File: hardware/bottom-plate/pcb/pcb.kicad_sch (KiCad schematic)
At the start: 83 parts, among them SW1 MT-0-102-A101-M200-RS+PJ, SW2 TS4535TP 250GF 009, SW3 TS4535TP 250GF 009

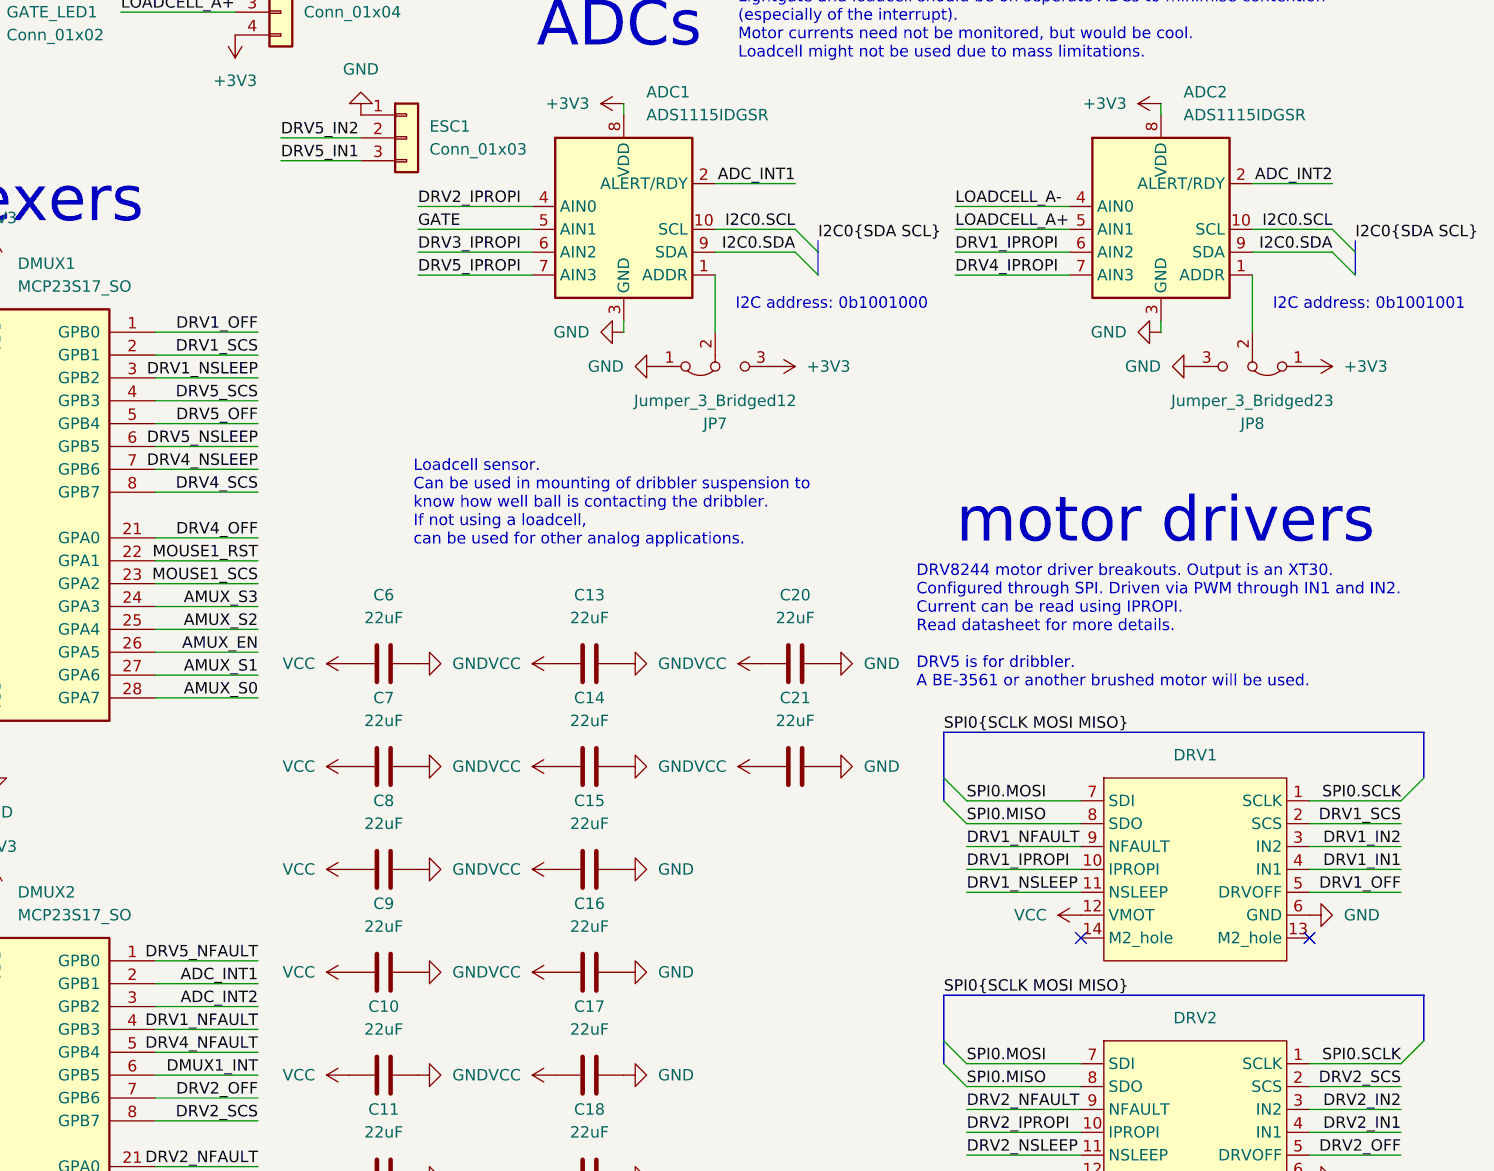
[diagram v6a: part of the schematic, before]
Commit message: fixed up cmake v2, added bottom pcb pinmaps, fixed bottom pcb pin naming in schematic
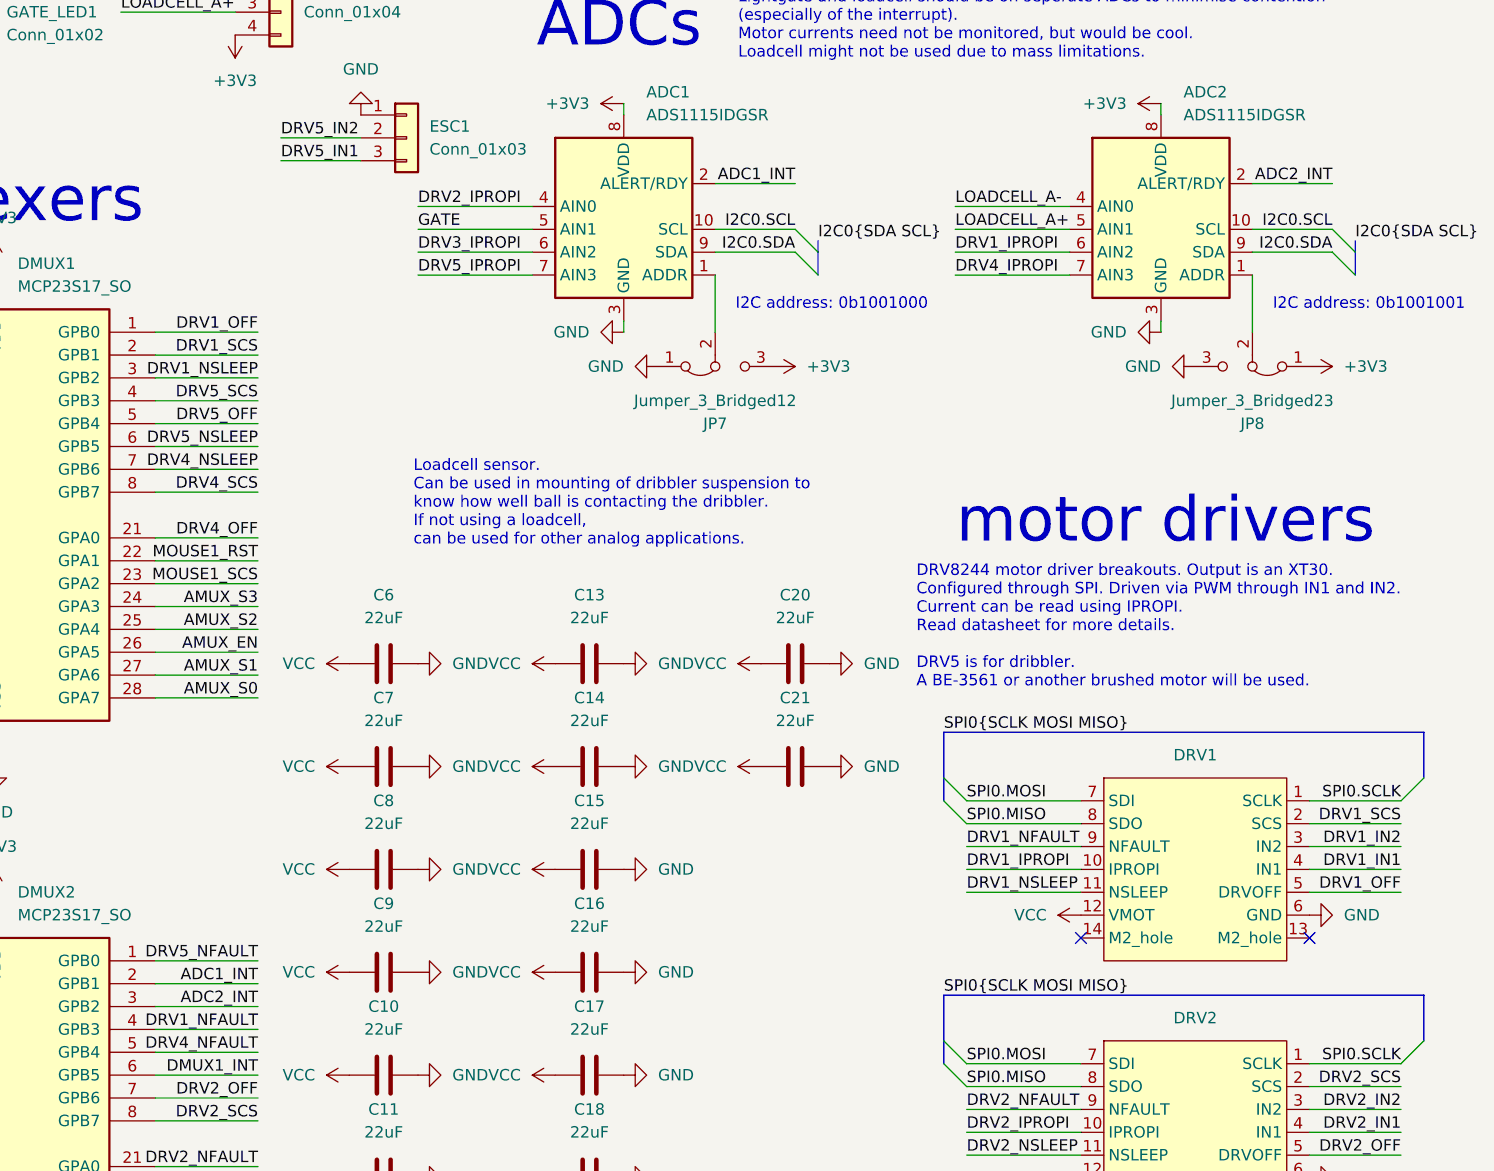
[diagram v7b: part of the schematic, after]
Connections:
- net ADC_INT1 renamed ADC1_INT
- net ADC_INT2 renamed ADC2_INT
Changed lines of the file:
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@@
 		)
 	)
-	(label "ADC_INT2"
+	(label "ADC2_INT"
 		(at 184.15 135.89 180)
 		(effects
@@
 		)
 	)
-	(label "ADC_INT2"
+	(label "ADC2_INT"
 		(at 303.53 44.45 180)
 		(effects
@@
 		)
 	)
-	(label "ADC_INT1"
+	(label "ADC1_INT"
 		(at 184.15 133.35 180)
 		(effects
@@
 		)
 	)
-	(label "ADC_INT1"
+	(label "ADC1_INT"
 		(at 243.84 44.45 180)
 		(effects

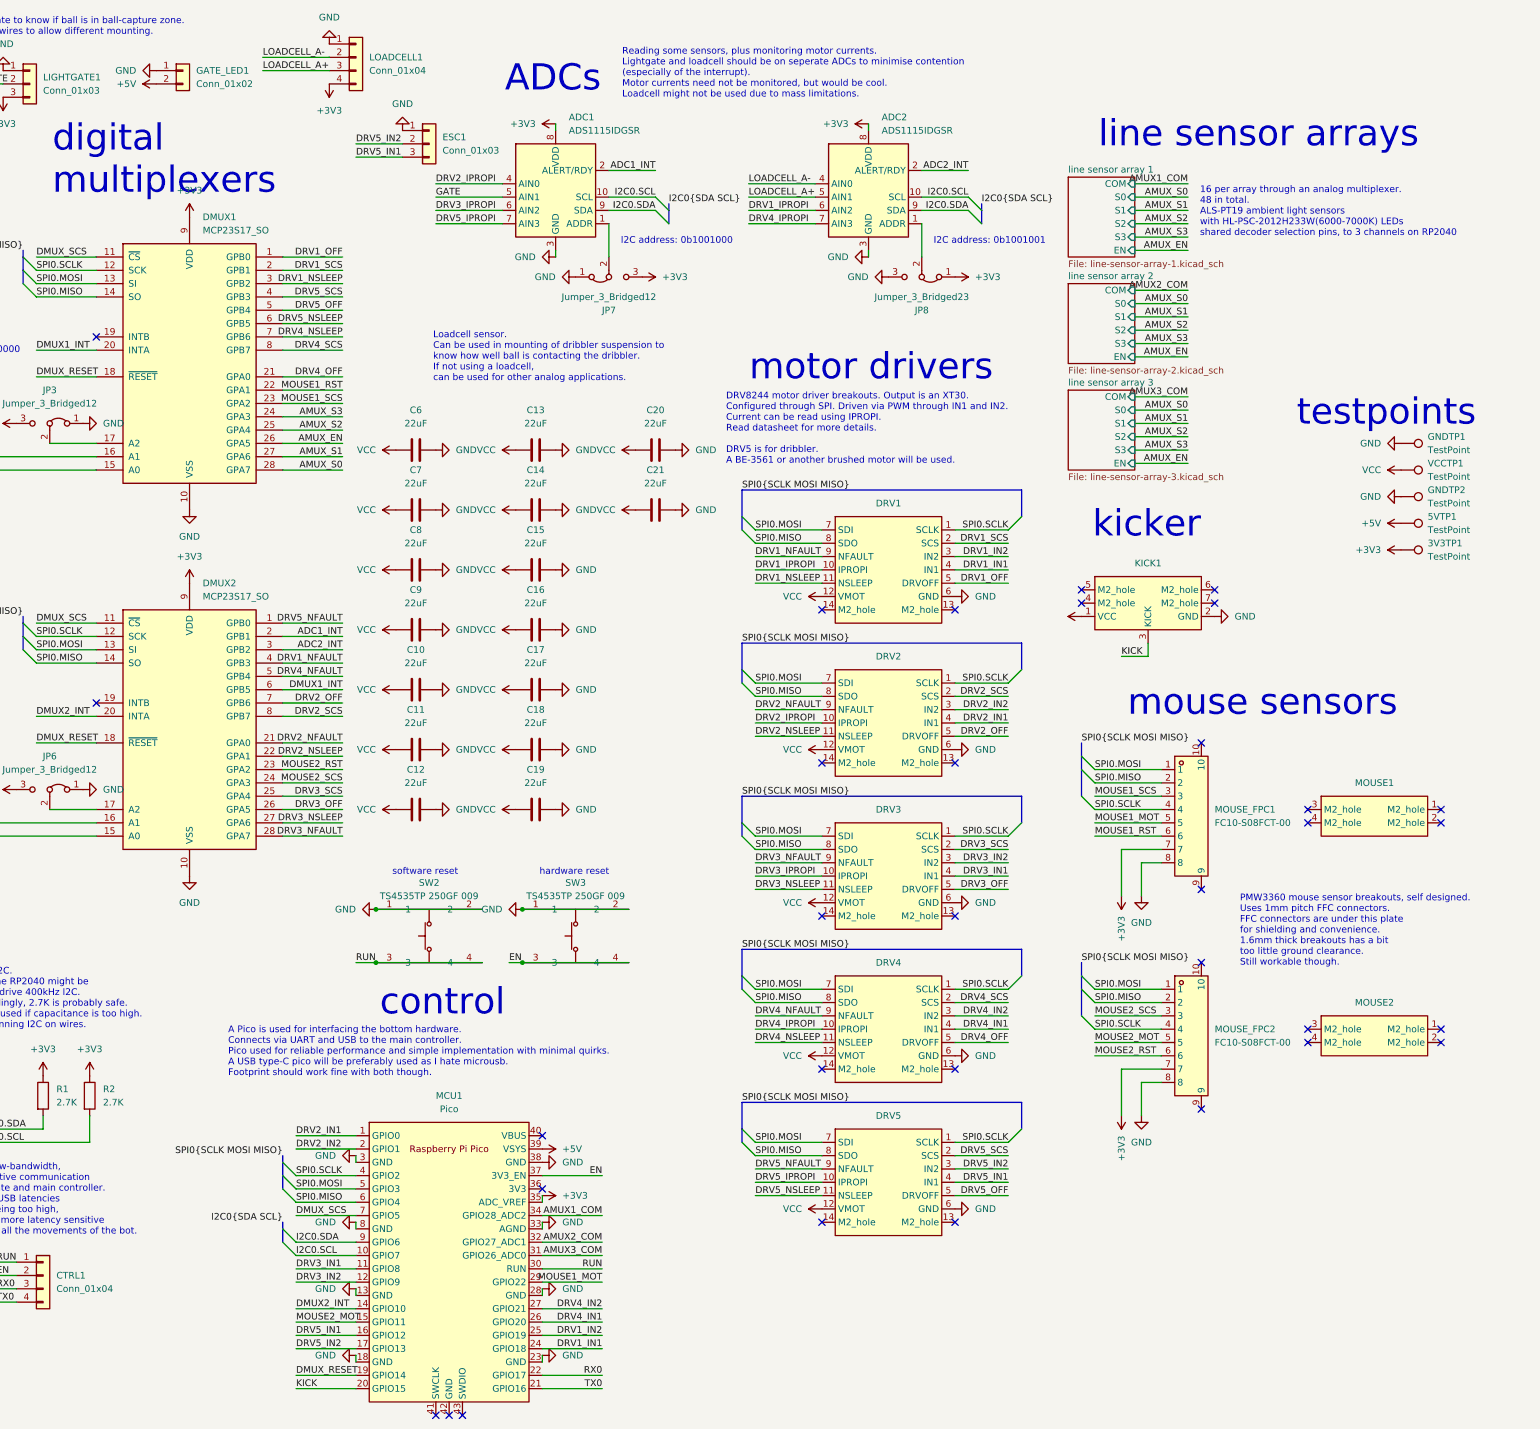
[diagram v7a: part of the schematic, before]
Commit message: bottom pcb fixed, im stupid
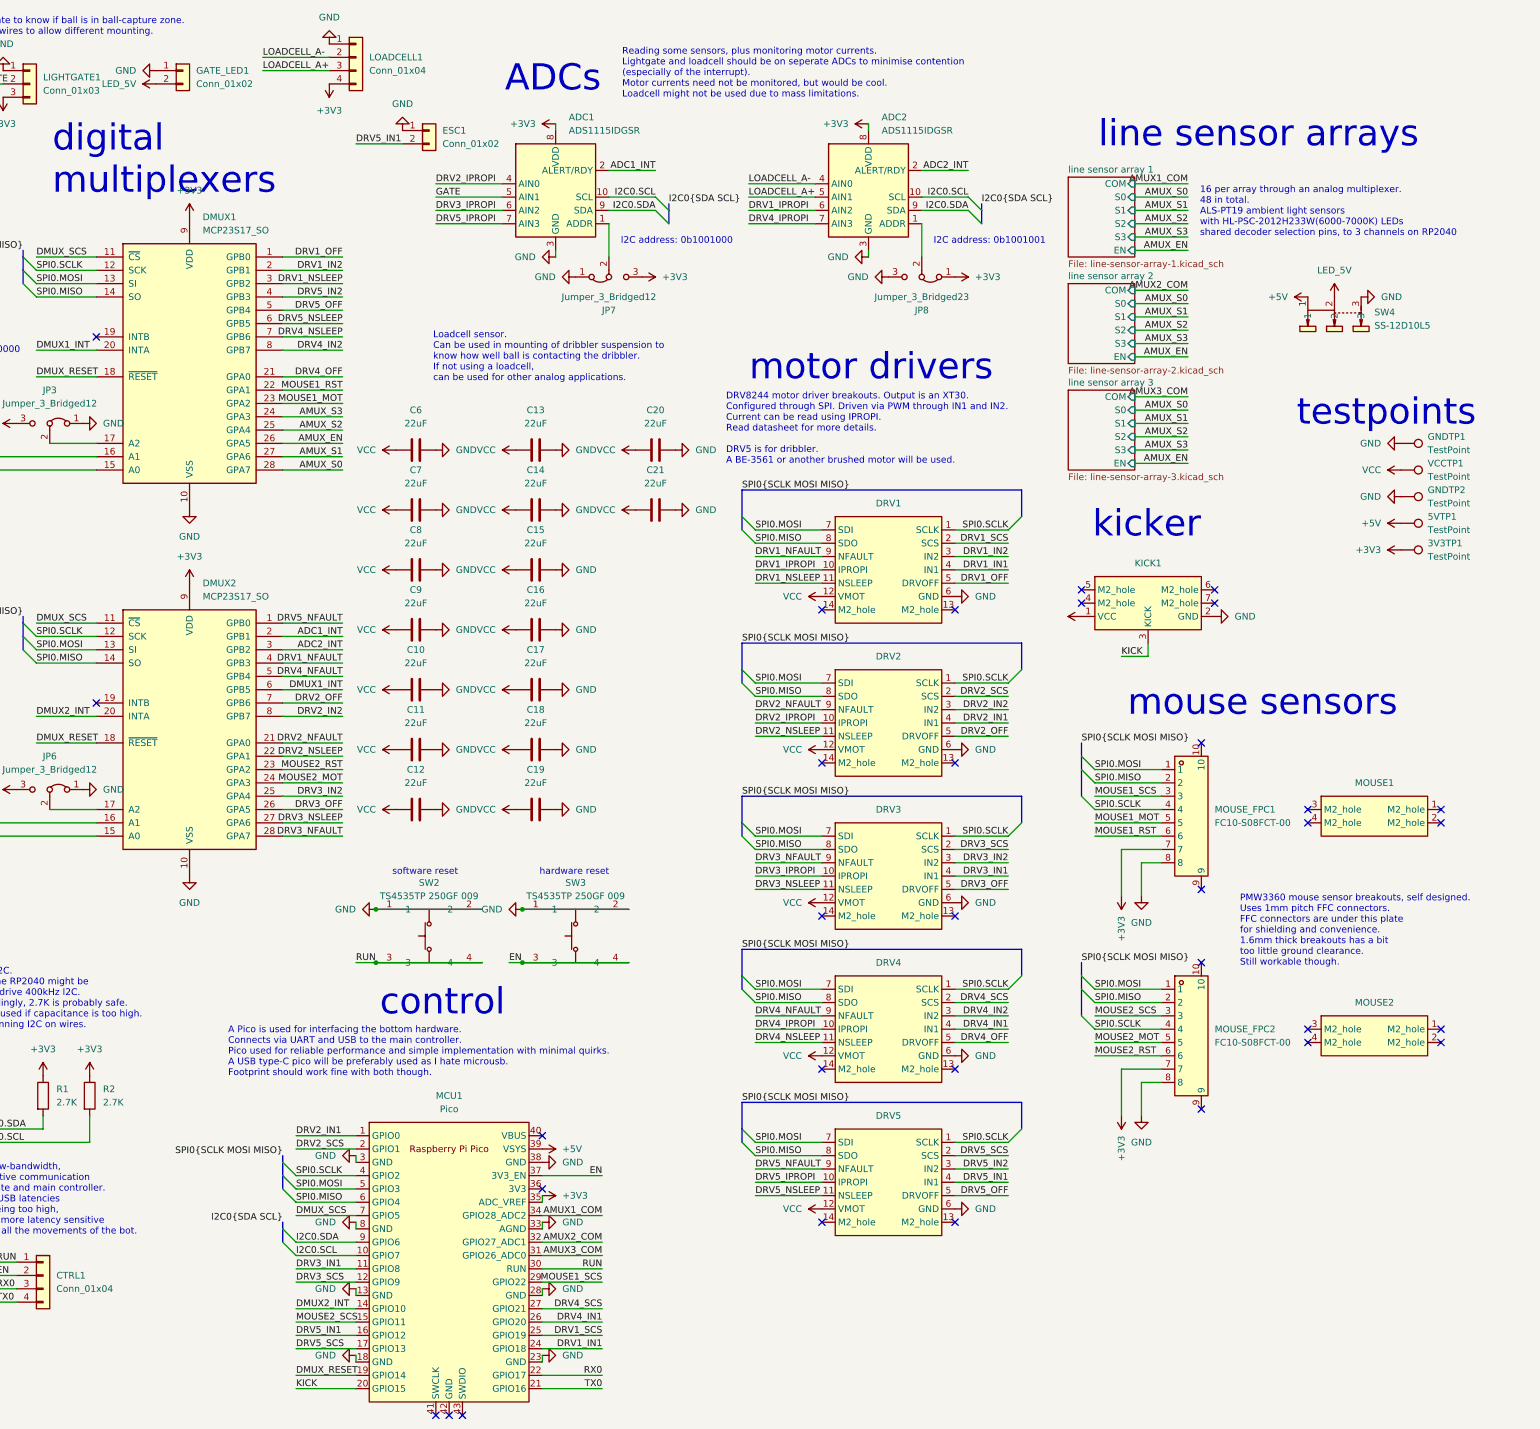
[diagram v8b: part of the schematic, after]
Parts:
- removed ESC1: Conn_01x03, Connector_JST:JST_XH_B3B-XH-A_1x03_P2.50mm_Vertical, symbol Connector_Generic:Conn_01x03
- added ESC1: Conn_01x02, Connector_JST:JST_XH_B2B-XH-A_1x02_P2.50mm_Vertical, symbol PCM_4ms_Connector:Conn_01x02
- added SW4: SS-12D10L5, EasyEDA:SW-TH_SS-12D10L5, symbol EasyEDA:SS-12D10L5
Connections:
- net +5V: now also SW4.1; no longer GATE_LED1.2 (Pin_2)
- net DRV1_IN2: now also DMUX1.2 (GPB1); no longer MCU1.25 (GPIO19)
- net DRV1_SCS: now also MCU1.25 (GPIO19); no longer DMUX1.2 (GPB1)
- net DRV2_IN2: now also DMUX2.8 (GPB7); no longer MCU1.2 (GPIO1)
- net DRV2_SCS: now also MCU1.2 (GPIO1); no longer DMUX2.8 (GPB7)
- net DRV3_IN2: now also DMUX2.25 (GPA4); no longer MCU1.12 (GPIO9)
- net DRV3_SCS: now also MCU1.12 (GPIO9); no longer DMUX2.25 (GPA4)
- net DRV4_IN2: now also DMUX1.8 (GPB7); no longer MCU1.27 (GPIO21)
- net DRV4_SCS: now also MCU1.27 (GPIO21); no longer DMUX1.8 (GPB7)
- net DRV5_IN1: now also ESC1.2 (Pin_2)
- net DRV5_IN2: now also DMUX1.4 (GPB3); no longer MCU1.17 (GPIO13)
- net DRV5_SCS: now also MCU1.17 (GPIO13); no longer DMUX1.4 (GPB3)
- net GND: now also ESC1.1 (Pin_1), SW4.3
- net MOUSE1_MOT: now also DMUX1.23 (GPA2); no longer MCU1.29 (GPIO22)
- net MOUSE1_SCS: now also MCU1.29 (GPIO22); no longer DMUX1.23 (GPA2)
- net MOUSE2_MOT: now also DMUX2.24 (GPA3); no longer MCU1.15 (GPIO11)
- net MOUSE2_SCS: now also MCU1.15 (GPIO11); no longer DMUX2.24 (GPA3)
- new net LED_5V: GATE_LED1.2 (Pin_2), SW4.2
